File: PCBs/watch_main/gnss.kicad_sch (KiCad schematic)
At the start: 1 part, among them IC401 TESEO-LIV4FTR

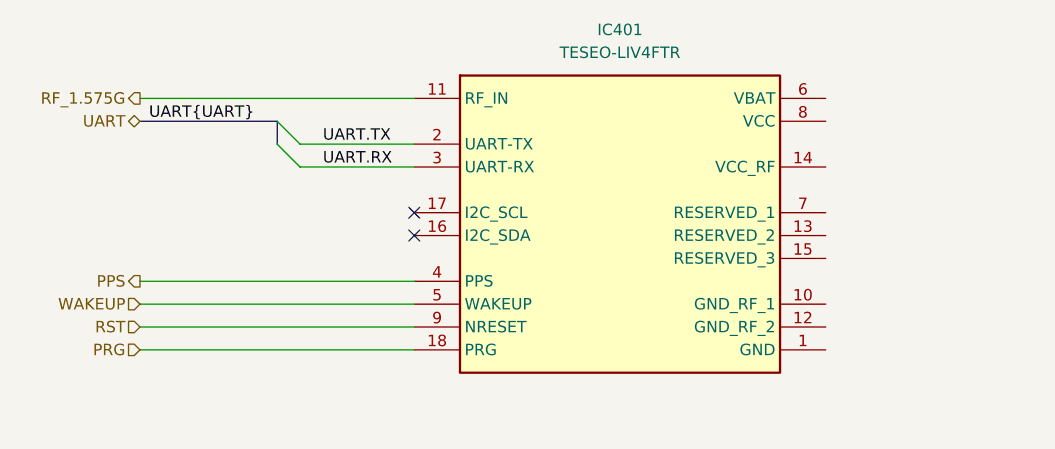
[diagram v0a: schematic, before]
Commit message: Created firmware project
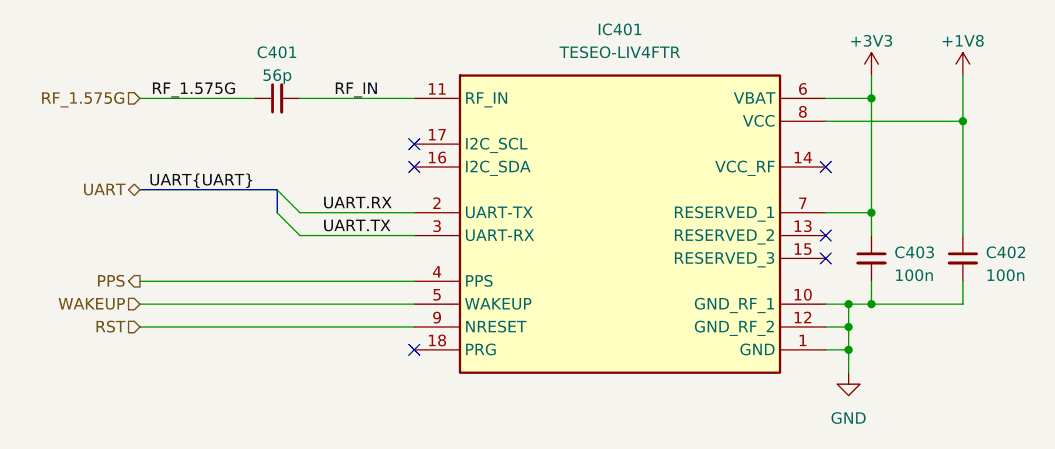
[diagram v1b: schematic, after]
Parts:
- added C401: 56p, Capacitor_SMD:C_0402_1005Metric, symbol Device:C_Small
- added C402, C403: 100n, Capacitor_SMD:C_0402_1005Metric, symbol Device:C_Small
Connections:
- net RF_1.575G: now also C401.1; no longer IC401.11 (RF_IN)
- net UART.RX: now also IC401.2 (UART-TX); no longer IC401.3 (UART-RX)
- net UART.TX: now also IC401.3 (UART-RX); no longer IC401.2 (UART-TX)
- net GND: now reaches IC401.1 (GND)
- net GND: now also IC401.10 (GND_RF_1), IC401.12 (GND_RF_2), C402.2, C403.2
- net +3V3: now reaches IC401.6 (VBAT)
- net +3V3: now also IC401.7 (RESERVED_1), C403.1
- net +1V8: now reaches IC401.8 (VCC)
- net +1V8: now also C402.1
- net PRG: no longer names the net of IC401.18 (PRG)
- new net RF_IN: C401.2, IC401.11 (RF_IN)
- no-connect marks 2 -> 6

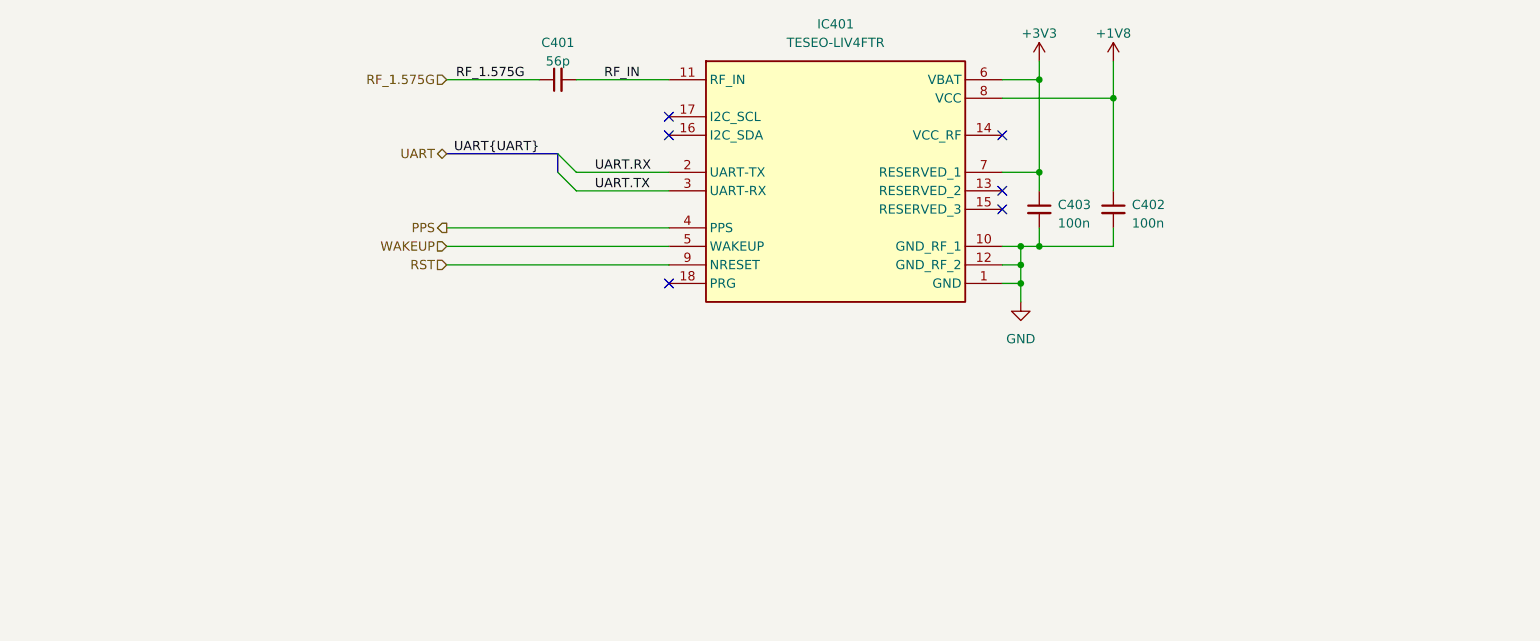
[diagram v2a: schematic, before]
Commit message: Schematic finished and BOM started
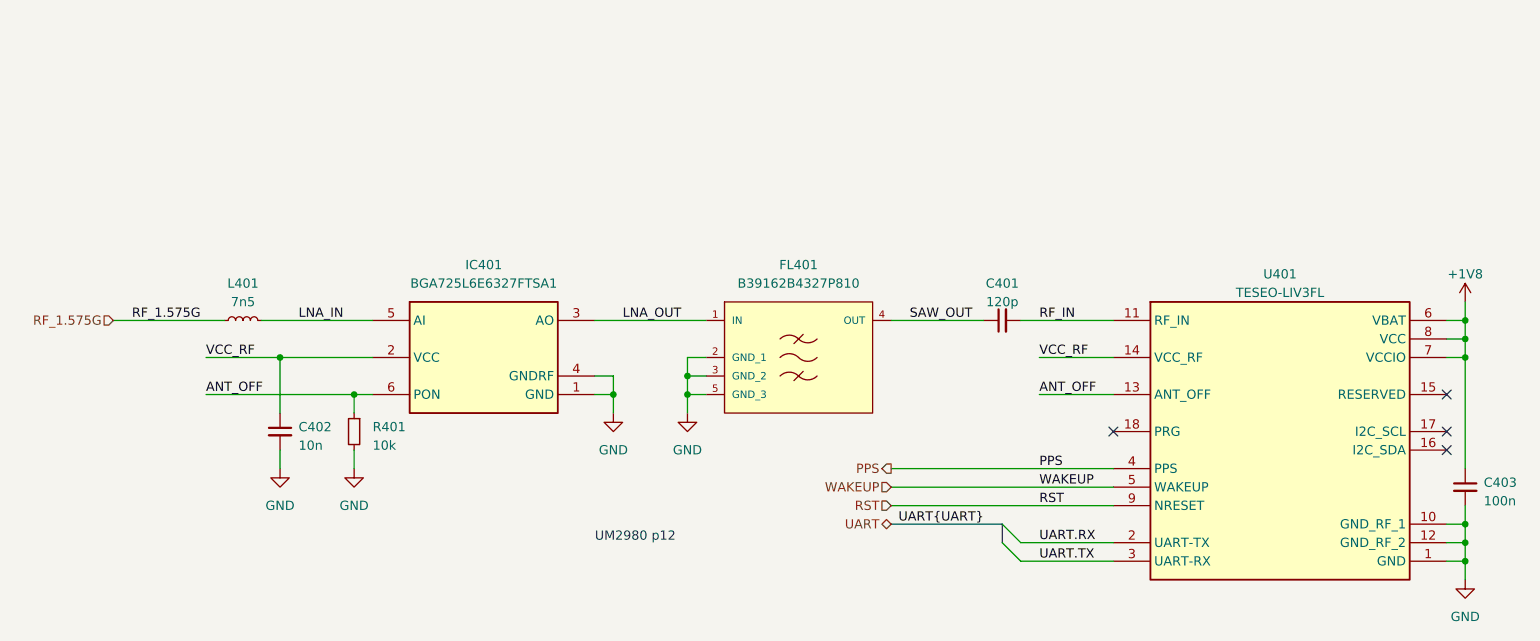
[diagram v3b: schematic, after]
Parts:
- removed IC401: TESEO-LIV4FTR, TESEOLIV4FTR, symbol TESEO-LIV4FTR:TESEO-LIV4FTR
- added FL401: B39162B4327P810, watch_footprints:B39162B4327P810, symbol B39162B4327P810:B39162B4327P810
- added IC401: BGA725L6E6327FTSA1, watch_footprints:BGS12SN6E6327XTSA1, symbol BGA725L6E6327FTSA1:BGA725L6E6327FTSA1
- added L401: 7n5, Inductor_SMD:L_0402_1005Metric, symbol Device:L_Small
- added R401: 10k, Resistor_SMD:R_0402_1005Metric, symbol Device:R_Small
- added U401: TESEO-LIV3FL, watch_footprints:TESEOLIV3FL, symbol TESEO-LIV3FL:TESEO-LIV3FL
- C401: value 56p -> 120p
- C402: value 100n -> 10n
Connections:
- net +3V3 is gone; now on net +1V8: C403.1
- net +1V8: now also U401.6 (VBAT), U401.7 (VCCIO), U401.8 (VCC); no longer C402.1
- net GND: now also FL401.2 (GND_1), FL401.3 (GND_2), FL401.5 (GND_3), IC401.1 (GND), IC401.4 (GNDRF), R401.2, U401.1 (GND), U401.10 (GND_RF_1), U401.12 (GND_RF_2)
- net PPS: now also U401.4 (PPS)
- net RF_1.575G: now also L401.1; no longer C401.1
- net RF_IN: now also U401.11 (RF_IN)
- net RST: now also U401.9 (NRESET)
- net UART.RX: now also U401.2 (UART-TX)
- net UART.TX: now also U401.3 (UART-RX)
- net WAKEUP: now also U401.5 (WAKEUP)
- new net ANT_OFF: IC401.6 (PON), R401.1, U401.13 (ANT_OFF)
- new net LNA_IN: IC401.5 (AI), L401.2
- new net LNA_OUT: FL401.1 (IN), IC401.3 (AO)
- new net SAW_OUT: C401.1, FL401.4 (OUT)
- new net VCC_RF: C402.1, IC401.2 (VCC), U401.14 (VCC_RF)
- no-connect marks 6 -> 4
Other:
- note added: "UM2980 p12"
- title: (none) -> Watch GNSS

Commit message: Started routing main PCB
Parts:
- renumbered C402 to C401, C401 to C402
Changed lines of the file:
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@@
     (effects (font (size 1.27 1.27)) (justify right))
+  )
+  (netclass_flag "" (length 2.54) (shape round) (at 53.34 81.28 0) (fields_autoplaced)
+    (effects (font (size 1.27 1.27)) (justify left bottom))
+    (property "Netclass" "50Ω RF" (at 54.0385 78.74 0)
+      (effects (font (size 1.27 1.27) italic) (justify left))
+    )
+  )
+  (netclass_flag "" (length 2.54) (shape round) (at 160.02 81.28 0) (fields_autoplaced)
+    (effects (font (size 1.27 1.27)) (justify left bottom))
+    (property "Netclass" "50Ω RF" (at 160.7185 78.74 0)
+      (effects (font (size 1.27 1.27) italic) (justify left))
+    )
+  )
+  (netclass_flag "" (length 2.54) (shape round) (at 177.8 81.28 0) (fields_autoplaced)
+    (effects (font (size 1.27 1.27)) (justify left bottom))
+    (property "Netclass" "50Ω RF" (at 178.4985 78.74 0)
+      (effects (font (size 1.27 1.27) italic) (justify left))
+    )
   )
   (netclass_flag "" (length 2.54) (shape round) (at 76.2 81.28 0) (fields_autoplaced)
     (effects (font (size 1.27 1.27)) (justify left bottom))
-    (property "Netclass" "50Ω MS SE" (at 76.8985 78.74 0)
-      (effects (font (size 1.27 1.27) italic) (justify left))
-    )
-  )
-  (netclass_flag "" (length 2.54) (shape round) (at 53.34 81.28 0) (fields_autoplaced)
-    (effects (font (size 1.27 1.27)) (justify left bottom))
-    (property "Netclass" "50Ω MS SE" (at 54.0385 78.74 0)
-      (effects (font (size 1.27 1.27) italic) (justify left))
-    )
-  )
-  (netclass_flag "" (length 2.54) (shape round) (at 177.8 81.28 0) (fields_autoplaced)
-    (effects (font (size 1.27 1.27)) (justify left bottom))
-    (property "Netclass" "50Ω MS SE" (at 178.4985 78.74 0)
-      (effects (font (size 1.27 1.27) italic) (justify left))
-    )
-  )
-  (netclass_flag "" (length 2.54) (shape round) (at 160.02 81.28 0) (fields_autoplaced)
-    (effects (font (size 1.27 1.27)) (justify left bottom))
-    (property "Netclass" "50Ω MS SE" (at 160.7185 78.74 0)
+    (property "Netclass" "50Ω RF" (at 76.8985 78.74 0)
       (effects (font (size 1.27 1.27) italic) (justify left))
     )
@@
   (netclass_flag "" (length 2.54) (shape round) (at 119.38 81.28 0) (fields_autoplaced)
     (effects (font (size 1.27 1.27)) (justify left bottom))
-    (property "Netclass" "50Ω MS SE" (at 120.0785 78.74 0)
+    (property "Netclass" "50Ω RF" (at 120.0785 78.74 0)
       (effects (font (size 1.27 1.27) italic) (justify left))
     )
@@
   (symbol (lib_id "Device:C_Small") (at 175.26 81.28 90) (unit 1)
     (in_bom yes) (on_board yes) (dnp no)
-    (property "Reference" "C401" (at 175.2663 76.2 90)
+    (property "Reference" "C402" (at 175.2663 76.2 90)
       (effects (font (size 1.27 1.27)))
     )
@@
       (project "watch_main"
         (path "/b008648a-c7cf-4e14-8a0a-b9314d757b4a/5b4d8e40-7178-4a95-9fb2-854856b4b577"
-          (reference "C401") (unit 1)
+          (reference "C402") (unit 1)
         )
       )
@@
   (symbol (lib_id "Device:C_Small") (at 76.2 96.52 0) (unit 1)
     (in_bom yes) (on_board yes) (dnp no) (fields_autoplaced)
-    (property "Reference" "C402" (at 78.74 95.8913 0)
+    (property "Reference" "C401" (at 78.74 95.8913 0)
       (effects (font (size 1.27 1.27)) (justify left))
     )
@@
       (project "watch_main"
         (path "/b008648a-c7cf-4e14-8a0a-b9314d757b4a/5b4d8e40-7178-4a95-9fb2-854856b4b577"
-          (reference "C402") (unit 1)
+          (reference "C401") (unit 1)
         )
       )
@@
   (symbol (lib_id "power:GND") (at 86.36 101.6 0) (unit 1)
     (in_bom yes) (on_board yes) (dnp no) (fields_autoplaced)
-    (property "Reference" "#PWR0406" (at 86.36 107.95 0)
+    (property "Reference" "#PWR0402" (at 86.36 107.95 0)
       (effects (font (size 1.27 1.27)) hide)
     )
@@
       (project "watch_main"
         (path "/b008648a-c7cf-4e14-8a0a-b9314d757b4a/5b4d8e40-7178-4a95-9fb2-854856b4b577"
-          (reference "#PWR0406") (unit 1)
+          (reference "#PWR0402") (unit 1)
         )
       )
@@
   (symbol (lib_id "power:GND") (at 132.08 93.98 0) (unit 1)
     (in_bom yes) (on_board yes) (dnp no) (fields_autoplaced)
-    (property "Reference" "#PWR0405" (at 132.08 100.33 0)
+    (property "Reference" "#PWR0404" (at 132.08 100.33 0)
       (effects (font (size 1.27 1.27)) hide)
     )
@@
       (project "watch_main"
         (path "/b008648a-c7cf-4e14-8a0a-b9314d757b4a/5b4d8e40-7178-4a95-9fb2-854856b4b577"
+          (reference "#PWR0404") (unit 1)
+        )
+      )
+    )
+  )
+  (symbol (lib_id "power:GND") (at 238.76 116.84 0) (unit 1)
+    (in_bom yes) (on_board yes) (dnp no) (fields_autoplaced)
+    (property "Reference" "#PWR0406" (at 238.76 123.19 0)
+      (effects (font (size 1.27 1.27)) hide)
+    )
+    (property "Value" "GND" (at 238.76 121.92 0)
+      (effects (font (size 1.27 1.27)))
+    )
+    (property "Footprint" "" (at 238.76 116.84 0)
+      (effects (font (size 1.27 1.27)) hide)
+    )
+    (property "Datasheet" "" (at 238.76 116.84 0)
+      (effects (font (size 1.27 1.27)) hide)
+    )
+    (pin "1")
+    (instances
+      (project "watch_main"
+        (path "/b008648a-c7cf-4e14-8a0a-b9314d757b4a/5b4d8e40-7178-4a95-9fb2-854856b4b577"
+          (reference "#PWR0406") (unit 1)
+        )
+      )
+    )
+  )
+  (symbol (lib_id "power:+1V8") (at 238.76 78.74 0) (unit 1)
+    (in_bom yes) (on_board yes) (dnp no) (fields_autoplaced)
+    (property "Reference" "#PWR0405" (at 238.76 82.55 0)
+      (effects (font (size 1.27 1.27)) hide)
+    )
+    (property "Value" "+1V8" (at 238.76 74.93 0)
+      (effects (font (size 1.27 1.27)))
+    )
+    (property "Footprint" "" (at 238.76 78.74 0)
+      (effects (font (size 1.27 1.27)) hide)
+    )
+    (property "Datasheet" "" (at 238.76 78.74 0)
+      (effects (font (size 1.27 1.27)) hide)
+    )
+    (pin "1")
+    (instances
+      (project "watch_main"
+        (path "/b008648a-c7cf-4e14-8a0a-b9314d757b4a/5b4d8e40-7178-4a95-9fb2-854856b4b577"
           (reference "#PWR0405") (unit 1)
         )
       )
-    )
-  )
-  (symbol (lib_id "power:GND") (at 238.76 116.84 0) (unit 1)
-    (in_bom yes) (on_board yes) (dnp no) (fields_autoplaced)
-    (property "Reference" "#PWR0404" (at 238.76 123.19 0)
-      (effects (font (size 1.27 1.27)) hide)
-    )
-    (property "Value" "GND" (at 238.76 121.92 0)
-      (effects (font (size 1.27 1.27)))
-    )
-    (property "Footprint" "" (at 238.76 116.84 0)
-      (effects (font (size 1.27 1.27)) hide)
-    )
-    (property "Datasheet" "" (at 238.76 116.84 0)
-      (effects (font (size 1.27 1.27)) hide)
-    )
-    (pin "1")
-    (instances
-      (project "watch_main"
-        (path "/b008648a-c7cf-4e14-8a0a-b9314d757b4a/5b4d8e40-7178-4a95-9fb2-854856b4b577"
-          (reference "#PWR0404") (unit 1)
-        )
-      )
-    )
-  )
-  (symbol (lib_id "power:+1V8") (at 238.76 78.74 0) (unit 1)
-    (in_bom yes) (on_board yes) (dnp no) (fields_autoplaced)
-    (property "Reference" "#PWR0402" (at 238.76 82.55 0)
-      (effects (font (size 1.27 1.27)) hide)
-    )
-    (property "Value" "+1V8" (at 238.76 74.93 0)
-      (effects (font (size 1.27 1.27)))
-    )
-    (property "Footprint" "" (at 238.76 78.74 0)
-      (effects (font (size 1.27 1.27)) hide)
-    )
-    (property "Datasheet" "" (at 238.76 78.74 0)
-      (effects (font (size 1.27 1.27)) hide)
-    )
-    (pin "1")
-    (instances
-      (project "watch_main"
-        (path "/b008648a-c7cf-4e14-8a0a-b9314d757b4a/5b4d8e40-7178-4a95-9fb2-854856b4b577"
-          (reference "#PWR0402") (unit 1)
-        )
-      )
